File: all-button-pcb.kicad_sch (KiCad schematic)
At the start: 22 parts, among them SW1 SW_SPST, SW2 SW_SPST, SW3 SW_SPST, U1 rp2040-zero

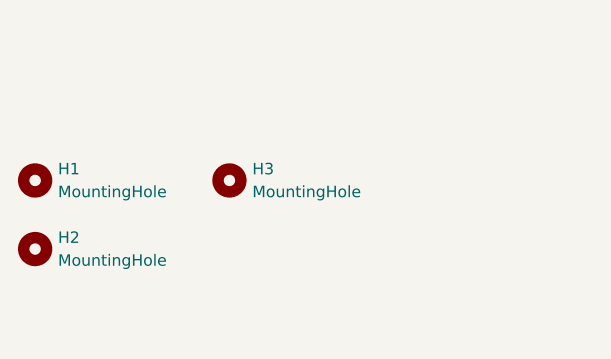
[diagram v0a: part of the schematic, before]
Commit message: supportive holes
added supportive holes for corners to trim case
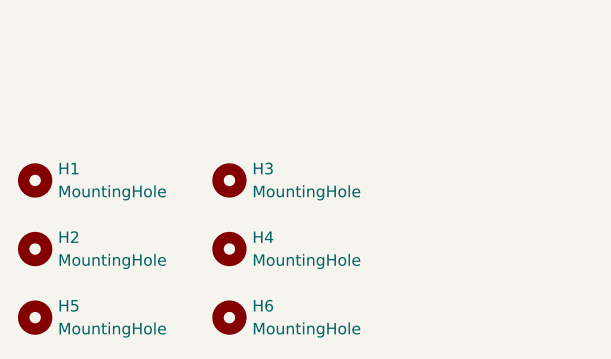
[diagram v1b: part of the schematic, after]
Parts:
- added H4, H5, H6: MountingHole, MountingHole:MountingHole_6.5mm, symbol Mechanical:MountingHole
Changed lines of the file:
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@@
+    )
+  )
+  (symbol (lib_id "Mechanical:MountingHole") (at 44.45 185.42 0) (unit 1)
+    (in_bom yes) (on_board yes) (dnp no) (fields_autoplaced)
+    (property "Reference" "H6" (at 46.99 184.15 0)
+      (effects (font (size 1.27 1.27)) (justify left))
+    )
+    (property "Value" "MountingHole" (at 46.99 186.69 0)
+      (effects (font (size 1.27 1.27)) (justify left))
+    )
+    (property "Footprint" "MountingHole:MountingHole_6.5mm" (at 44.45 185.42 0)
+      (effects (font (size 1.27 1.27)) hide)
+    )
+    (property "Datasheet" "~" (at 44.45 185.42 0)
+      (effects (font (size 1.27 1.27)) hide)
+    )
+    (instances
+      (project "all-button-pcb"
+        (path "/3f74d14b-4e67-47b3-994e-3634c96e2b2b"
+          (reference "H6") (unit 1)
+        )
+      )
     )
   )
@@
         (path "/3f74d14b-4e67-47b3-994e-3634c96e2b2b"
           (reference "#PWR016") (unit 1)
+        )
+      )
+    )
+  )
+  (symbol (lib_id "Mechanical:MountingHole") (at 44.45 177.8 0) (unit 1)
+    (in_bom yes) (on_board yes) (dnp no) (fields_autoplaced)
+    (property "Reference" "H4" (at 46.99 176.53 0)
+      (effects (font (size 1.27 1.27)) (justify left))
+    )
+    (property "Value" "MountingHole" (at 46.99 179.07 0)
+      (effects (font (size 1.27 1.27)) (justify left))
+    )
+    (property "Footprint" "MountingHole:MountingHole_6.5mm" (at 44.45 177.8 0)
+      (effects (font (size 1.27 1.27)) hide)
+    )
+    (property "Datasheet" "~" (at 44.45 177.8 0)
+      (effects (font (size 1.27 1.27)) hide)
+    )
+    (instances
+      (project "all-button-pcb"
+        (path "/3f74d14b-4e67-47b3-994e-3634c96e2b2b"
+          (reference "H4") (unit 1)
         )
       )
@@
         )
       )
+    )
+  )
+  (symbol (lib_id "Mechanical:MountingHole") (at 22.86 185.42 0) (unit 1)
+    (in_bom yes) (on_board yes) (dnp no) (fields_autoplaced)
+    (property "Reference" "H5" (at 25.4 184.15 0)
+      (effects (font (size 1.27 1.27)) (justify left))
+    )
+    (property "Value" "MountingHole" (at 25.4 186.69 0)
+      (effects (font (size 1.27 1.27)) (justify left))
+    )
+    (property "Footprint" "MountingHole:MountingHole_6.5mm" (at 22.86 185.42 0)
+      (effects (font (size 1.27 1.27)) hide)
+    )
+    (property "Datasheet" "~" (at 22.86 185.42 0)
+      (effects (font (size 1.27 1.27)) hide)
+    )
+    (instances
+      (project "all-button-pcb"
+        (path "/3f74d14b-4e67-47b3-994e-3634c96e2b2b"
+          (reference "H5") (unit 1)
+        )
+      )
